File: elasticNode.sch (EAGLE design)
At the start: 137 parts, among them J1 FEMALE_HEADER_5X2, J10 USB_CONNMICRO_SMT, J11 JTAG_CONN_6PINSMT, J2 FEMALE_HEADER_5X2, J3 ISP_CONN_6PIN, J4 FEMALE_HEADER_2X1, J5 JUMPER, J6 ISP_CONN_6PIN, J7 JUMPER, J8 USB_CONNMICRO_SMT, J9 FEMALE_HEADER_10X2, M1 SISS23DN, M2 SISS23DN, M3 SISS23DN, M4 SISS23DN, U1 AT90USB128, U10 PAC1720, U11 LTC3419DFN, U12 LTC3419DFN, U2 MRF24J40MA, U3 ATMEGA32U4QFN, U4 IS66WV51216EALL, U5 SPARTAN7-LX15, U6 SST26VF032BWDFN, U7 PAC1720, U8 PAC1720, U9 PAC1720, X1 8MHz, X2 8MHz, X3 100MHz, X4 50MHz, X5 32MHz

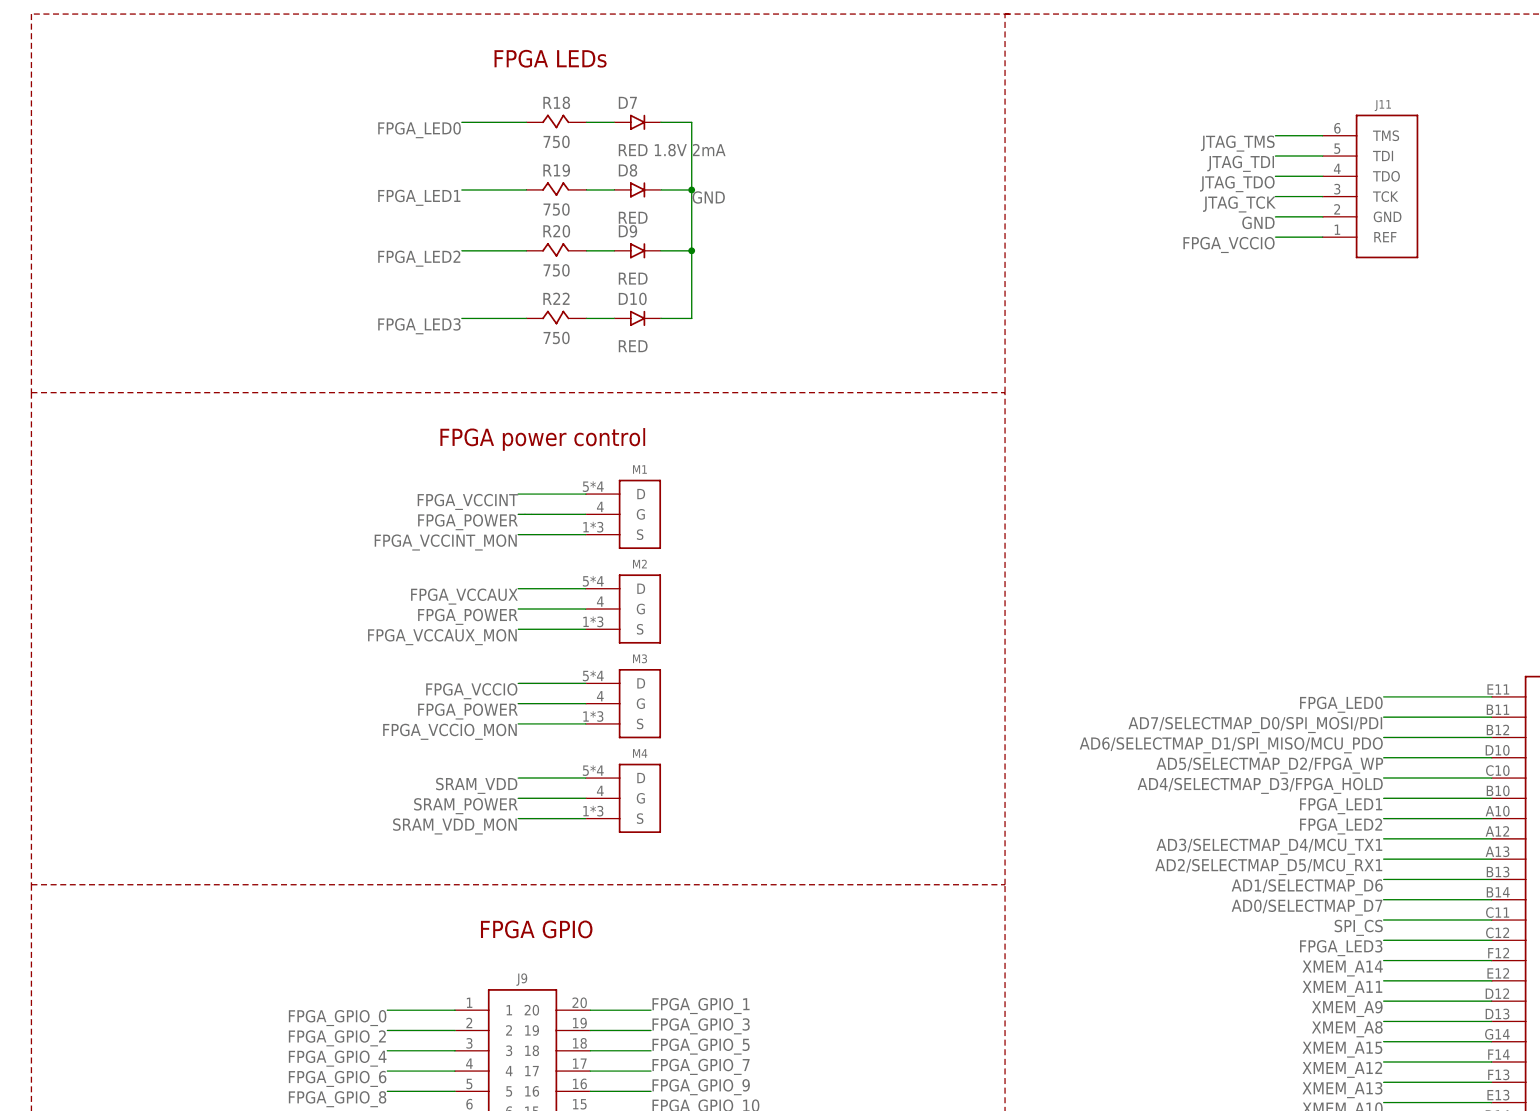
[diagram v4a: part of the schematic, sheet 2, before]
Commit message: renumber all elements.
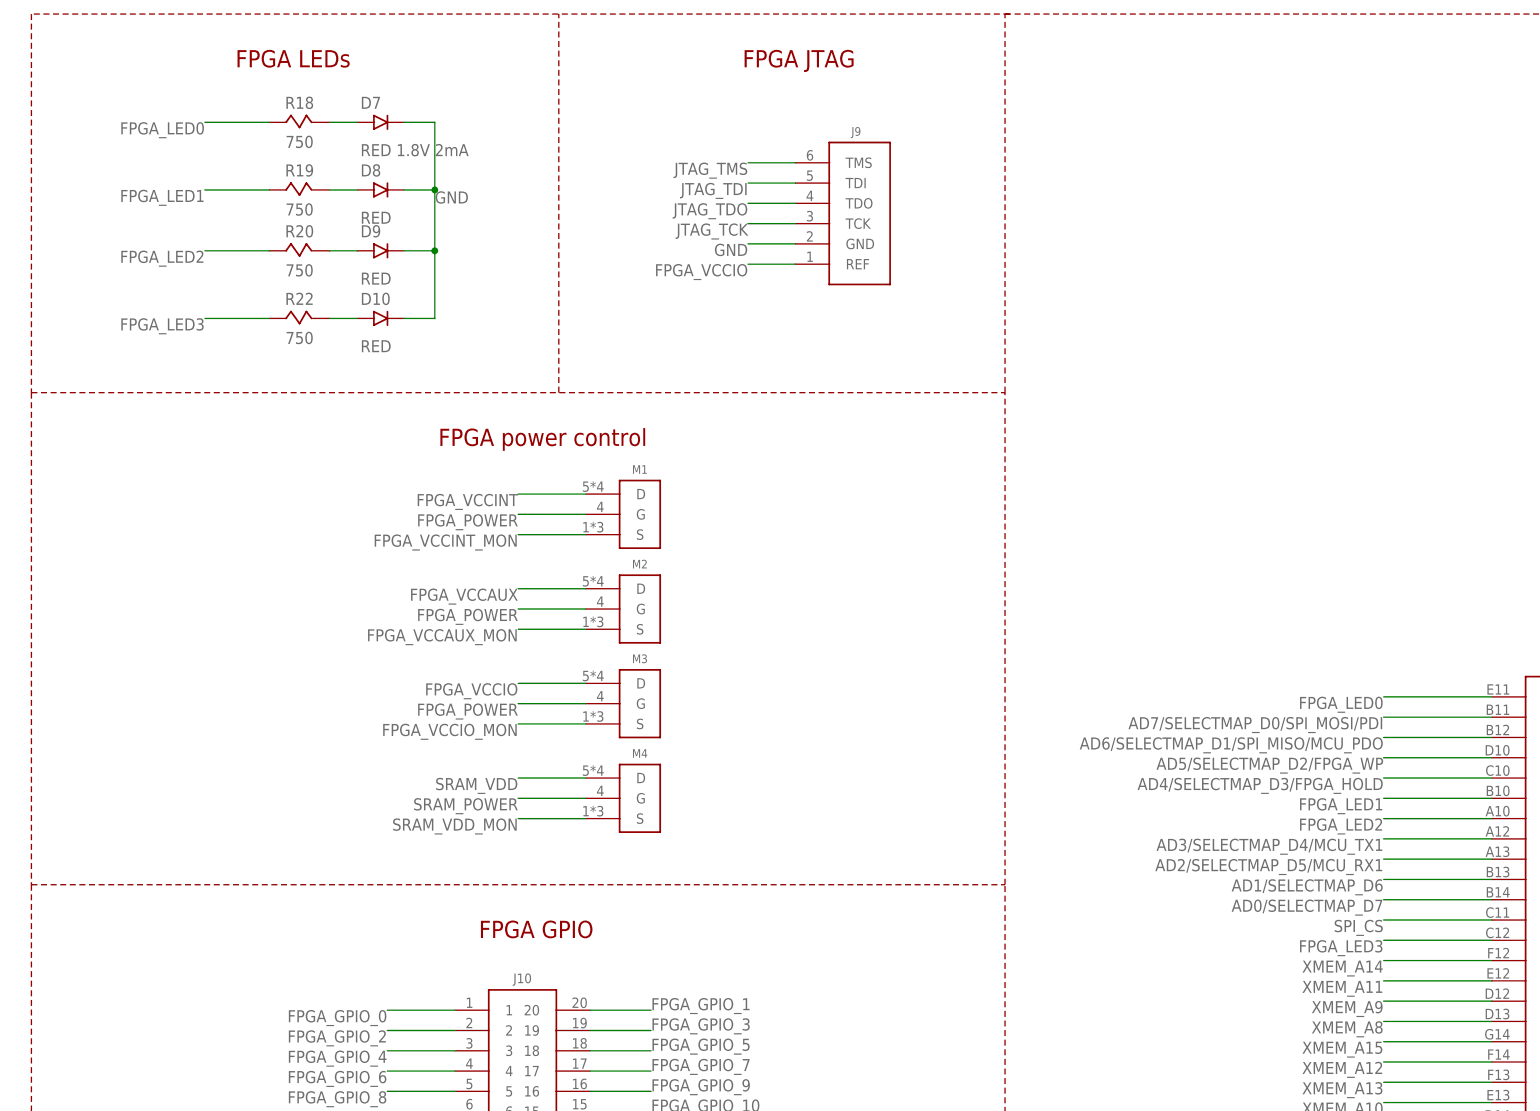
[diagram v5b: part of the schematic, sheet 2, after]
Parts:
- J10: value USB_CONNMICRO_SMT -> FEMALE_HEADER_10X2; device connectors:USB_CONNMICRO_SMT -> connectors:FEMALE_HEADER_10X2
- J11: value JTAG_CONN_6PINSMT -> USB_CONNMICRO_SMT; device connectors:JTAG_CONN_6PINSMT -> connectors:USB_CONNMICRO_SMT
- J9: value FEMALE_HEADER_10X2 -> JTAG_CONN_6PINSMT; device connectors:FEMALE_HEADER_10X2 -> connectors:JTAG_CONN_6PINSMT
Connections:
- net FPGA_GPIO_0: now also J10.1; no longer J9.1
- net FPGA_GPIO_1: now also J10.20; no longer J9.20
- net FPGA_GPIO_10: now also J10.15; no longer J9.15
- net FPGA_GPIO_11: now also J10.6; no longer J9.6
- net FPGA_GPIO_12: now also J10.14; no longer J9.14
- net FPGA_GPIO_13: now also J10.7; no longer J9.7
- net FPGA_GPIO_14: now also J10.8; no longer J9.8
- net FPGA_GPIO_15: now also J10.13; no longer J9.13
- net FPGA_GPIO_16: now also J10.9; no longer J9.9
- net FPGA_GPIO_17: now also J10.12; no longer J9.12
- net FPGA_GPIO_18: now also J10.10; no longer J9.10
- net FPGA_GPIO_19: now also J10.11; no longer J9.11
- net FPGA_GPIO_2: now also J10.2; no longer J9.2
- net FPGA_GPIO_3: now also J10.19; no longer J9.19
- net FPGA_GPIO_4: now also J10.3; no longer J9.3
- net FPGA_GPIO_5: now also J10.18; no longer J9.18
- net FPGA_GPIO_6: now also J10.4; no longer J9.4
- net FPGA_GPIO_7: now also J10.17; no longer J9.17
- net FPGA_GPIO_8: now also J10.5; no longer J9.5
- net FPGA_GPIO_9: now also J10.16; no longer J9.16
- net FPGA_VCCIO: now also J9.REF; no longer J11.REF
- net GND: now also J9.GND; no longer J10.GND
- net JTAG_TCK: now also J9.TCK; no longer J11.TCK
- net JTAG_TDI: now also J9.TDI; no longer J11.TDI
- net JTAG_TDO: now also J9.TDO; no longer J11.TDO
- net JTAG_TMS: now also J9.TMS; no longer J11.TMS
- net UID: now also J11.UID; no longer J10.UID
- net USBD+: now also J11.D+; no longer J10.D+
- net USBD-: now also J11.D-; no longer J10.D-
- net USB_VCC_RAW: now also J11.VCC; no longer J10.VCC
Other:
- note added: "FPGA JTAG"
- moved on the sheet: D10, D7, D8, D9, R18, R19, R20, R22

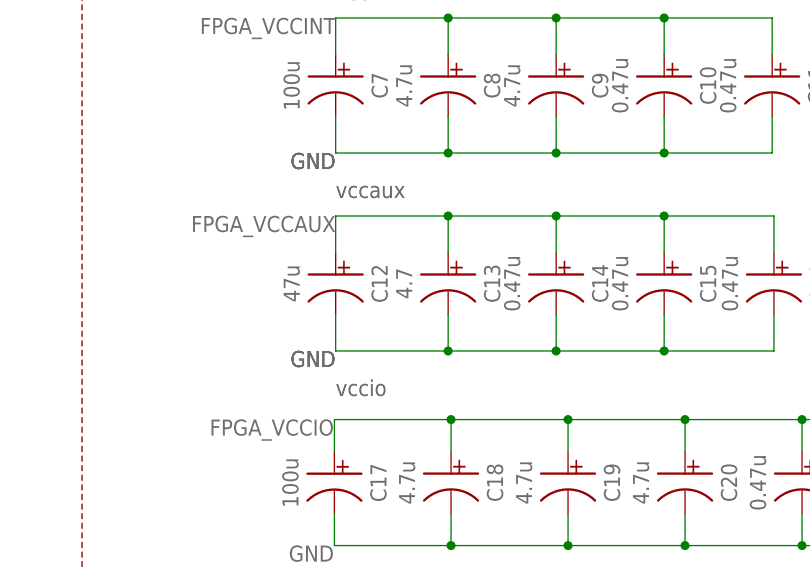
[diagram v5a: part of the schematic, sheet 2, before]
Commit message: fix mistake about the capacitor of 4.7uF
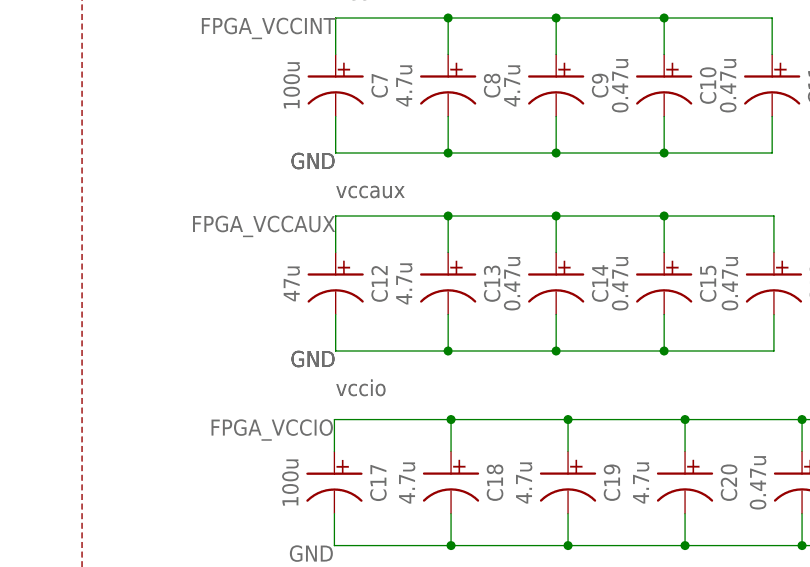
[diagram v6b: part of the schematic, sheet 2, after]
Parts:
- C13: value 4.7 -> 4.7u
- C8: device passive:CAPACITOR1210 -> passive:CAPACITOR0805

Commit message: Change the 100M clock signals connection
Add enable signal to oscillator 100M, and check aux IOs Voltage.
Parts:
- added R49: 270, passive:RESISTOR
- R23: value 2.4k -> 15k
- R27: value 15k -> 2.4k
- R28: value 1.5k -> 15k
- R30: value 0.8 -> 1.5k
- R31, R33: value .8 -> 0.8
- R32: value 0.8 -> .8
- R34: value 100 -> .8
- R35: value 2000 -> 100
- R36: value .8 -> 2000
- R38: value 0.15 -> .8
- R39: value .8 -> 0.15
- R40: value 750 -> .8
- R41: value 300 -> 750
- R42: value 6k8 -> 300
- R43, R47: value 10k -> 6k8
- R44: value 20k -> 10k
- R45: value 1k5 -> 20k
- R46: value 6k8 -> 1k5
- R48: value 270 -> 10k
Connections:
- new net EN_OSC_100: R23.1, U1.(PCINT7/OC.0A/OC.1C)PB7, X3.EN
- net 1V: now also R40.2, R44.2; no longer R39.2, R43.2
- net 1V8: now also R31.2, R38.2, R45.1; no longer R30.2, R37.2, R44.1
- net 3V3: now also R27.1, R30.2, R34.2, R37.2, R43.2; no longer R26.1, R28.2, R31.2, R36.2, R42.2
- net 5V: now also R39.2; no longer R38.2
- net DAUGHTER_VCC: now also R32.1; no longer R31.1
- net FPGA_LED2: now also U5.IO_L6N_T0_D08_VREF_14; no longer U5.IO_L3N_T0_DQS_EMCCLK_14
- net FPGA_LED3: now also U5.IO_L20P_T3_D24_14; no longer U5.IO_L6N_T0_D08_VREF_14
- net FPGA_RESET: now also R28.1; no longer R27.1
- net FPGA_VCCAUX: no longer R21.2, R25.1, R27.2, X4.EN, X4.VS+, X5.EN, X5.VS+
- net FPGA_VCCAUX_MON: now also R38.1; no longer R37.1
- net FPGA_VCCINT_MON: now also R40.1; no longer R39.1
- net FPGA_VCCIO: now also R21.2, R23.2, R25.1, R26.1, R28.2, X3.VS+, X4.EN, X4.VS+, X5.EN, X5.VS+; no longer R23.1
- net FPGA_VCCIO_MON: now also R33.1; no longer R32.1
- net GND: now also R36.1, R42.1, R47.2, R49.1; no longer R34.1, R40.1, R45.2, R47.1
- net MCU_VCC: now also R34.1; no longer R33.1
- net MODE0: now also R24.2; no longer R23.2
- net MODE1: now also R25.2; no longer R24.2
- net MODE2: now also R26.2; no longer R25.2
- net N$11: now also R41.2; no longer R40.2
- net N$12: now also R35.2; no longer R34.2
- net N$14: now also R36.2; no longer R35.2
- net N$2: now also R44.1, R47.1; no longer R43.1, R46.1
- net N$28: now also R49.2; no longer R48.2
- net N$53: now also R43.1, R46.1; no longer R42.1, R45.1
- net N$7: now also R45.2, R48.2; no longer R44.2, R47.2
- net N$9: now also R42.2; no longer R41.2
- net OSC_100: now also U5.IO_L3N_T0_DQS_EMCCLK_14; no longer U5.IO_L12P_T1_MRCC_34
- net SCL: now also R29.1; no longer R28.1
- net SDA: now also R30.1; no longer R29.1
- net SPI_CS: now also R27.2; no longer R26.2
- net SRAM_VDD: no longer X3.EN, X3.VS+
- net SRAM_VDD_MON: now also R31.1; no longer R30.1
- net USB_VCC_RAW: now also R39.1; no longer R38.1
- net WIRELESS_VCC: now also R37.1; no longer R36.1
- net WIRELESS_WAKE: now also U1.PF1(ADC1); no longer U1.(PCINT7/OC.0A/OC.1C)PB7
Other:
- moved on the sheet: R23, R24, R25, R26, R27, R29, R30, R31, R32, R33, R34, R35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
